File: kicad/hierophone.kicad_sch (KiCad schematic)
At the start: 135 parts, among them J1 AudioJack2_SwitchT, J10 Conn_01x02, J11 Conn_01x02, J12 Conn_01x02, J2 AudioJack2_SwitchT, J4 AudioJack2_SwitchT, J5 AudioJack2_SwitchT, J6 AudioJack2_SwitchT, J7 AudioJack2_SwitchT, J9 Conn_01x02, Q1 2N3904, Q2 2N3906, Q3 2N3906, SW3 SW_SPDT, U10 TL072, U11 TL072, U12 TL072, U13 TL072, U2 LM13700, U3 LM13700, U4 TL072, U5 TL072, U6 LM386, U7 NE5534, U8 TL072

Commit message: Fixing name...
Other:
- title: Heirophone -> Hierophone

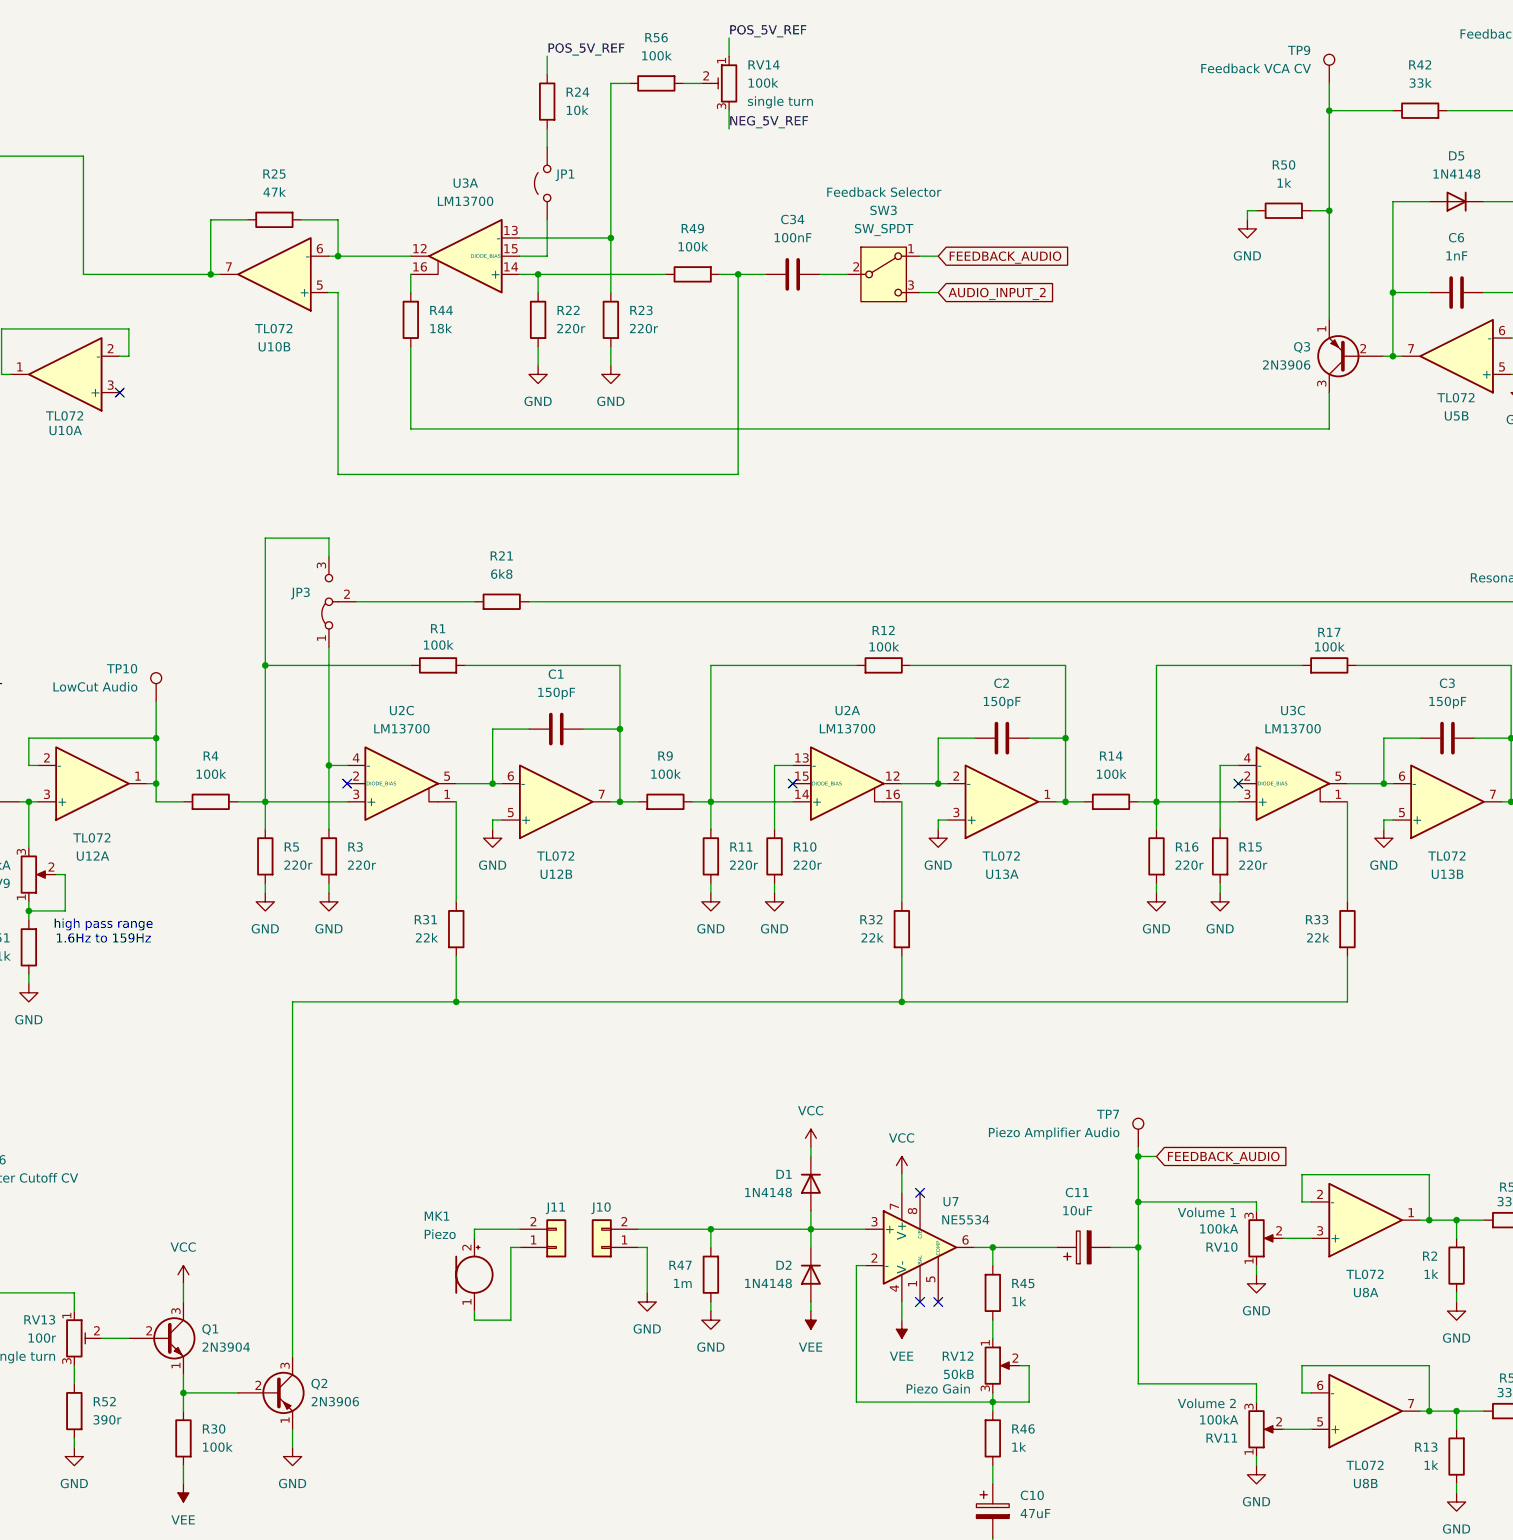
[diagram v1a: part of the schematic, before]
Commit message: Updating for KiCAD version 9
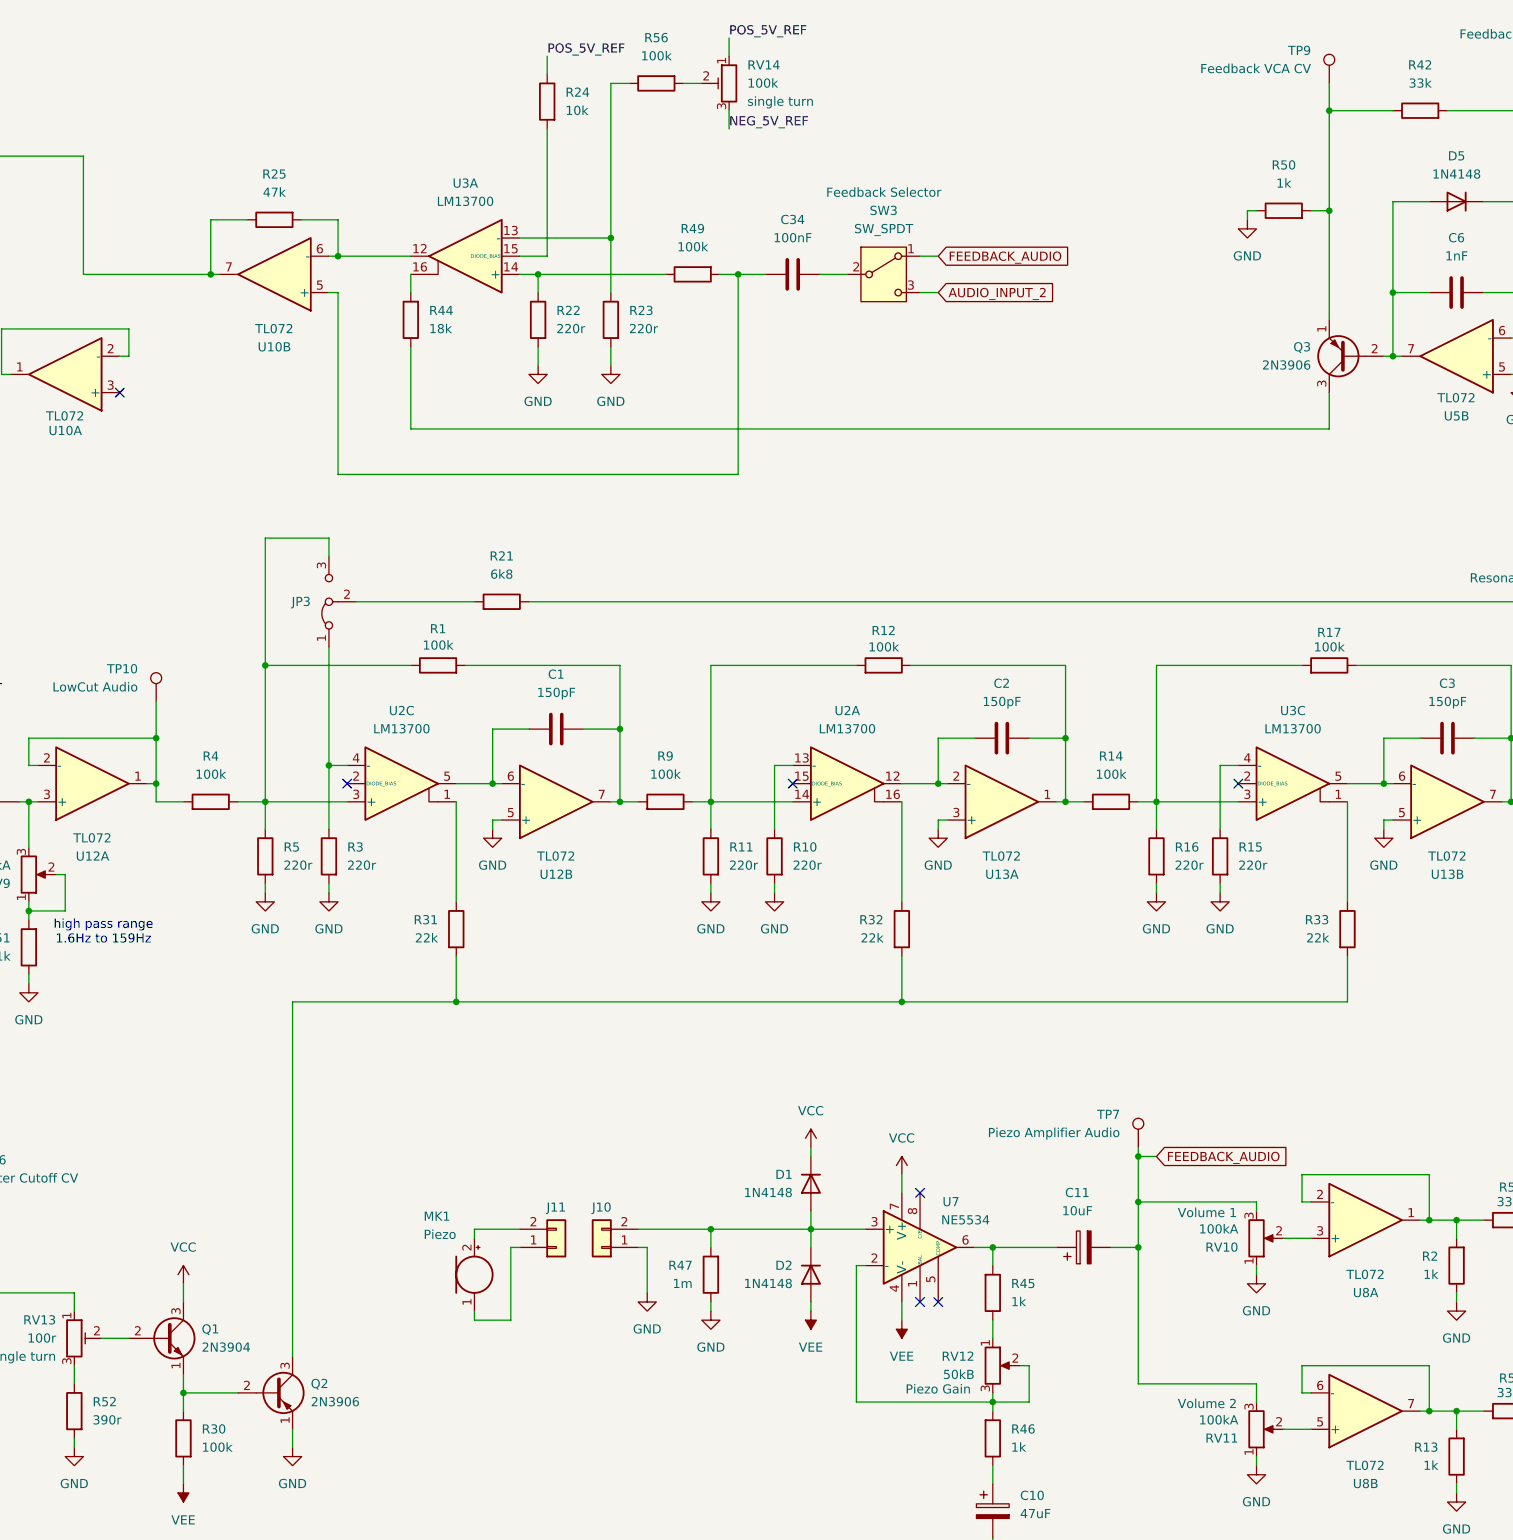
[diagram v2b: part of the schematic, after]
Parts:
- removed JP1: Jumper_2_Open, Connector_PinHeader_2.54mm:PinHeader_1x02_P2.54mm_Vertical, symbol Jumper:Jumper_2_Open
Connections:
- net at U3.15 (DIODE_BIAS): now also R24.1
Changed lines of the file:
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@@
 (kicad_sch
-	(version 20231120)
+	(version 20250114)
 	(generator "eeschema")
-	(generator_version "8.0")
+	(generator_version "9.0")
 	(paper "A3")
 	(title_block
@@
 		(comment 4 "Author: Guy John")
 	)
+	(text "high pass range\n1.6Hz to 159Hz"
+		(exclude_from_sim no)
+		(at 123.444 149.098 0)
+		(effects
+			(font
+				(size 1.27 1.27)
+			)
+		)
+	)
+	(text "Speaker"
+		(exclude_from_sim no)
+		(at 401.828 144.526 0)
+		(effects
+			(font
+				(size 1.27 1.27)
+			)
+		)
+	)
 	(junction
 		(at 138.43 57.15)
@@
 	(wire
 		(pts
-			(xy 185.42 49.53) (xy 185.42 54.61)
-		)
-		(stroke
-			(width 0)
-			(type default)
-		)
-	)
-	(wire
-		(pts
 			(xy 252.73 209.55) (xy 252.73 214.63)
 		)
@@
 	(wire
 		(pts
-			(xy 185.42 36.83) (xy 185.42 39.37)
+			(xy 185.42 36.83) (xy 185.42 54.61)
 		)
 		(stroke
@@
 		)
 	)
-	(text "high pass range\n1.6Hz to 159Hz"
-		(exclude_from_sim no)
-		(at 123.444 149.098 0)
-		(effects
-			(font
-				(size 1.27 1.27)
-			)
-		)
-	)
-	(text "Speaker"
-		(exclude_from_sim no)
-		(at 401.828 144.526 0)
-		(effects
-			(font
-				(size 1.27 1.27)
-			)
-		)
-	)
 	(label "POS_5V_REF"
 		(at 210.82 24.13 0)
@@
 	)
 	(symbol
-		(lib_id "Jumper:Jumper_2_Open")
-		(at 185.42 44.45 90)
-		(unit 1)
-		(exclude_from_sim yes)
-		(in_bom no)
-		(on_board yes)
-		(dnp no)
-		(fields_autoplaced yes)
-		(property "Reference" "JP1"
-			(at 186.69 43.1799 90)
-			(effects
-				(font
-					(size 1.27 1.27)
-				)
-				(justify right)
-			)
-		)
-		(property "Value" "Jumper_2_Open"
-			(at 186.69 45.7199 90)
-			(effects
-				(font
-					(size 1.27 1.27)
-				)
-				(justify right)
-				(hide yes)
-			)
-		)
-		(property "Footprint" "Connector_PinHeader_2.54mm:PinHeader_1x02_P2.54mm_Vertical"
-			(at 185.42 44.45 0)
-			(effects
-				(font
-					(size 1.27 1.27)
-				)
-				(hide yes)
-			)
-		)
-		(property "Datasheet" "~"
-			(at 185.42 44.45 0)
-			(effects
-				(font
-					(size 1.27 1.27)
-				)
-				(hide yes)
-			)
-		)
-		(property "Description" "Jumper, 2-pole, open"
-			(at 185.42 44.45 0)
-			(effects
-				(font
-					(size 1.27 1.27)
-				)
-				(hide yes)
-			)
-		)
-		(pin "2"
-		)
-		(pin "1"
-		)
-		(instances
-			(project ""
-				(path "/5b0acaca-dc50-4fa5-b146-164c1b9ad031"
-					(reference "JP1")
-					(unit 1)
-				)
-			)
-		)
-	)
-	(symbol
 		(lib_id "Device:Speaker")
 		(at 429.26 149.86 0)
@@
 			)
 		)
+		(property "Sim.Pins" "1=K 2=A"
+			(at 181.61 269.24 0)
+			(effects
+				(font
+					(size 1.27 1.27)
+				)
+				(hide yes)
+			)
+		)
 		(pin "1"
 		)
@@
 		(at 377.19 228.6 0)
 		(unit 1)
-		(exclude_from_sim yes)
+		(exclude_from_sim no)
 		(in_bom no)
 		(on_board yes)
@@
 		(at 367.03 228.6 0)
 		(unit 1)
-		(exclude_from_sim yes)
+		(exclude_from_sim no)
 		(in_bom no)
 		(on_board yes)
@@
 		(at 154.94 102.87 90)
 		(unit 1)
-		(exclude_from_sim yes)
+		(exclude_from_sim no)
 		(in_bom no)
 		(on_board yes)
@@
 		(fields_autoplaced yes)
 		(property "Reference" "JP3"
-			(at 152.4 101.5999 90)
+			(at 152.4 102.8699 90)
 			(effects
 				(font
@@
 		(at 372.11 228.6 0)
 		(unit 1)
-		(exclude_from_sim yes)
+		(exclude_from_sim no)
 		(in_bom no)
 		(on_board yes)
@@
 		(at 382.27 228.6 0)
 		(unit 1)
-		(exclude_from_sim yes)
+		(exclude_from_sim no)
 		(in_bom no)
 		(on_board yes)
@@
 		(at 200.66 252.73)
 		(size 38.1 25.4)
+		(exclude_from_sim no)
+		(in_bom yes)
+		(on_board yes)
+		(dnp no)
 		(fields_autoplaced yes)
 		(stroke
@@
 		)
 	)
+	(embedded_fonts no)
 )

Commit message: Tweaking PCB
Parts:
- removed C42, C43: 10uF, Rumblesan_Standard_Parts:CP_Radial_D5.0mm_P2.00mm, symbol Rumblesan_Standard_Parts:C_Polarized
- removed D6, D7: 5v1, Diode_THT:D_DO-41_SOD81_P10.16mm_Horizontal, symbol Device:D_Zener
- removed JP3: Jumper_3_Bridged12, Jumper:SolderJumper-3_P1.3mm_Bridged12_RoundedPad1.0x1.5mm, symbol Jumper:Jumper_3_Bridged12
- removed R26, R27: 1k, Rumblesan_Standard_Parts:R_Axial_DIN0207_L6.3mm_D2.5mm_P10.16mm_Horizontal, symbol Rumblesan_Standard_Parts:R
- added R58: 1k, Rumblesan_Standard_Parts:R_Axial_DIN0207_L6.3mm_D2.5mm_P10.16mm_Horizontal, symbol Rumblesan_Standard_Parts:R
- R18: value 22k -> 47k
- R19: value 47k -> 10k
- R38, R56: value 100k -> 220k
- R39, R41: value 100k -> 10k
- R42: value 33k -> 22k
- R50: value 1k -> 1k2
- R57: value 100k -> 1m
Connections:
- net GND: now also RV5.3; no longer RV5.1
- net POS_5V_REF: now also RV5.1; no longer RV5.3
- net at R39.1, U5.2 (-): now also RV7.3; no longer RV7.1
- net at C6.1, D5.1 (K), R40.1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: now also RV7.1, R58.1; no longer R42.1, RV7.3
- net at R21.1: now also R1.2, R4.2, R5.2, U2.3 (+)
- new net: R42.1, R58.2
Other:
- note added: "OTA current out = 19.2 * iabc * vIn * 220/(100k+220) vOut = vIn - (OTA current out * 47k) vOut = vIn - (vIn * iabc * 0.042 * 47k) vOut/vIn = Gain = 1 - iabc * 1974 CV of 0v = iabc of 0ma -> gain of 1 CV of 2.5v = iabc of 0.504ma -> gain of 0.005104 CV of 5v = iabc of 1.008ma -> gain of -0.989792"
- note added: "iabc = Vc/100k * (1k2 + 23k)/1k2 0v = 0ma 2.5v = 0.504ma 5v = 1.008ma"
- moved on the sheet: R21, R28, R42, R56, RV14, RV5, RV7, TP8

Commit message: Fixing issues with the inputs
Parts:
- removed R18: 47k, Rumblesan_Standard_Parts:R_Axial_DIN0207_L6.3mm_D2.5mm_P10.16mm_Horizontal, symbol Rumblesan_Standard_Parts:R
- removed U11: TL072, Package_DIP:DIP-8_W7.62mm_Socket, symbol Amplifier_Operational:TL072
- added C44: 22pF, Rumblesan_Standard_Parts:C_Rect_L7.0mm_W2.5mm_P5.00mm, symbol Rumblesan_Standard_Parts:C
- added R59, R60, R61: 100k, Rumblesan_Standard_Parts:R_Axial_DIN0207_L6.3mm_D2.5mm_P10.16mm_Horizontal, symbol Rumblesan_Standard_Parts:R
- added R62: 10k, Rumblesan_Standard_Parts:R_Axial_DIN0207_L6.3mm_D2.5mm_P10.16mm_Horizontal, symbol Rumblesan_Standard_Parts:R
- added U1: TL074, Package_DIP:DIP-14_W7.62mm_Socket, symbol Amplifier_Operational:TL074
- R13, R2: value 1k -> 10k; now not fitted
- RV13: Name (none) -> V/Oct Trimmer
- RV14: Name (none) -> CV rejection
- RV15: Name (none) -> Centre null
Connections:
- net AUDIO_INPUT_2: now also RV2.3, U1.6 (-), U1.7; no longer R8.1
- net GND: now also U6.3 (+), R59.1, R60.1, U1.10 (+), U1.12 (+); no longer U6.2 (-)
- net VCC: now also U1.4 (V+)
- net VEE: now also U1.11 (V-)
- net at RV8.2: now also U6.2 (-); no longer U6.3 (+)
- net at C35.2, R28.1, R6.1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: now also U1.13 (-)
- net at C33.1, C35.1, R6.2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: now also U1.14
- net at RV2.2: now also R8.1
- net at J2.T: now also R59.2, U1.5 (+); no longer RV2.3
- net at C4.2, TP5.1: now also R61.1
- net at J1.T: now also R60.2, U1.3 (+); no longer RV1.3
- net at RV8.3: now also C44.1, R62.2, U1.8
- new net: C44.2, R61.2, R62.1, U1.9 (-)
- new net: RV1.3, U1.1, U1.2 (-)
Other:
- moved on the sheet: C41, C7, C8, C9, J1, J12, J2, J9, LS1, R43, R55, R7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

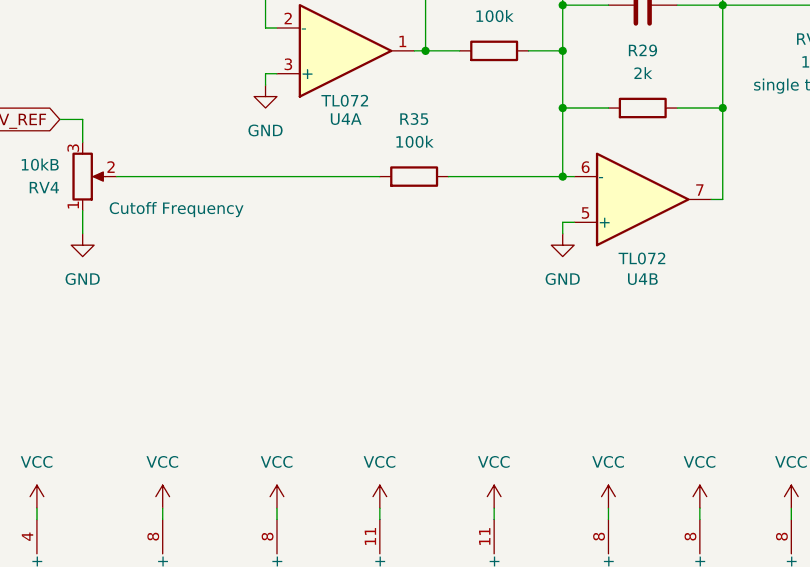
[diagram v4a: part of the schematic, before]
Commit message: Adding volt per octave input
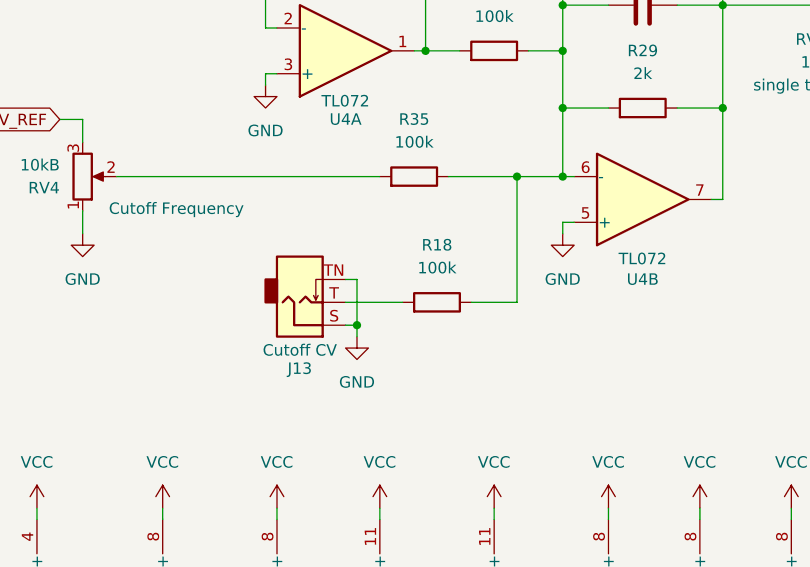
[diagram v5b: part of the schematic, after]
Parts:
- added J13: AudioJack2_SwitchT, Rumblesan_Audio_Connectors:Jack_3.5mm_QingPu_WQP-PJ398SM_Vertical, symbol Connector_Audio:AudioJack2_SwitchT
- added R18: 100k, Rumblesan_Standard_Parts:R_Axial_DIN0207_L6.3mm_D2.5mm_P10.16mm_Horizontal, symbol Rumblesan_Standard_Parts:R
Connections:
- net GND: now also J13.S, J13.TN
- net at C5.1, R29.1, R35.2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: now also R18.2
- new net: J13.T, R18.1

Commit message: More pcb tweaks
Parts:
- D4: Name (none) -> Power Indicator
- J10: Name (none) -> Pickup In
- J9: Name (none) -> PowerAmp Out
- RV1: Name (none) -> Input 1 Volume
- RV2: Name (none) -> Input 2 Volume
- RV9: Name (none) -> Low Cut
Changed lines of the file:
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@@
 			)
 		)
+		(property "Name" "Low Cut"
+			(at 113.03 140.97 0)
+			(effects
+				(font
+					(size 1.27 1.27)
+				)
+				(hide yes)
+			)
+		)
 		(pin "2"
 		)
@@
 			)
 		)
+		(property "Name" "PowerAmp Out"
+			(at 494.03 148.59 0)
+			(effects
+				(font
+					(size 1.27 1.27)
+				)
+				(hide yes)
+			)
+		)
 		(pin "1"
 		)
@@
 			)
 		)
+		(property "Name" "Input 2 Volume"
+			(at 63.5 128.27 0)
+			(effects
+				(font
+					(size 1.27 1.27)
+				)
+				(hide yes)
+			)
+		)
 		(pin "2"
 		)
@@
 			)
 		)
+		(property "Name" "Power Indicator"
+			(at 181.61 269.24 0)
+			(effects
+				(font
+					(size 1.27 1.27)
+				)
+				(hide yes)
+			)
+		)
 		(pin "1"
 		)
@@
 			)
 		)
+		(property "Name" "Input 1 Volume"
+			(at 63.5 91.44 0)
+			(effects
+				(font
+					(size 1.27 1.27)
+				)
+				(hide yes)
+			)
+		)
 		(pin "2"
 		)
@@
 			(at 193.04 193.04 0)
 			(effects
+				(font
+					(size 1.27 1.27)
+				)
+				(hide yes)
+			)
+		)
+		(property "Name" "Pickup In"
+			(at 193.04 193.04 0)
+			(effects

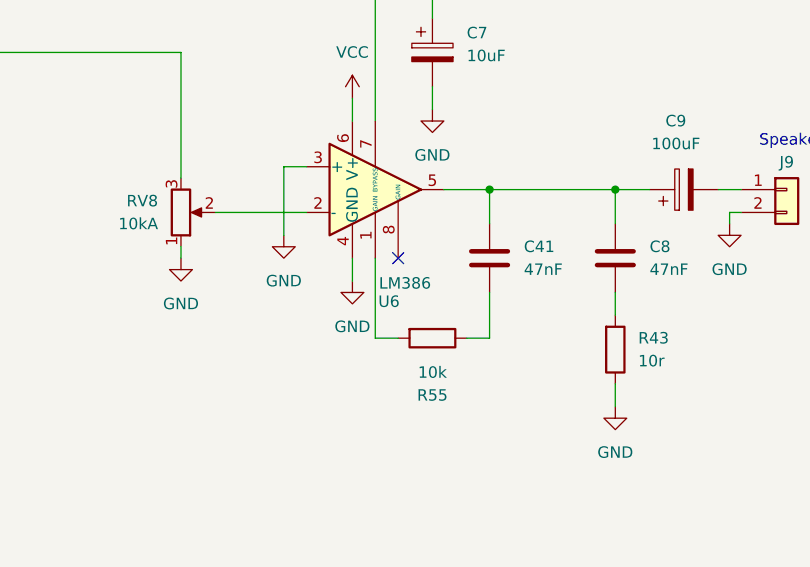
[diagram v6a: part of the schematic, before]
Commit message: Make sure to specify the lm386n-4
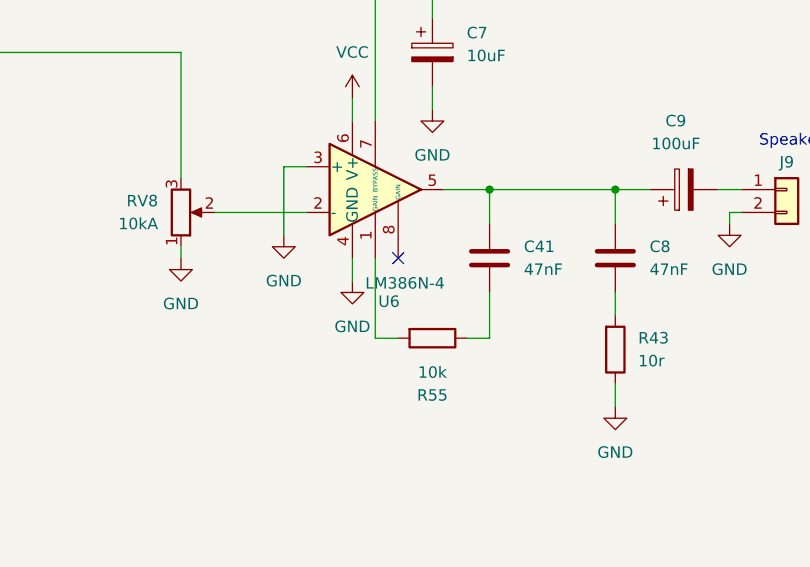
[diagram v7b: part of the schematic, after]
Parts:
- U6: value LM386 -> LM386N-4
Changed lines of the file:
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@@
 			)
 		)
-		(property "Value" "LM386"
+		(property "Value" "LM386N-4"
 			(at 451.612 159.004 0)
 			(effects
